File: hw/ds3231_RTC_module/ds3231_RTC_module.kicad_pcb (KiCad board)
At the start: 2 copper layers, 37 x 25 mm, 23 parts, among them J101 Conn_01x07, Q2101 AO3401A, Q2102 DMG1013T, U2101 DS3231M, U2102 CAT24C256, U2103 DS3231MZ

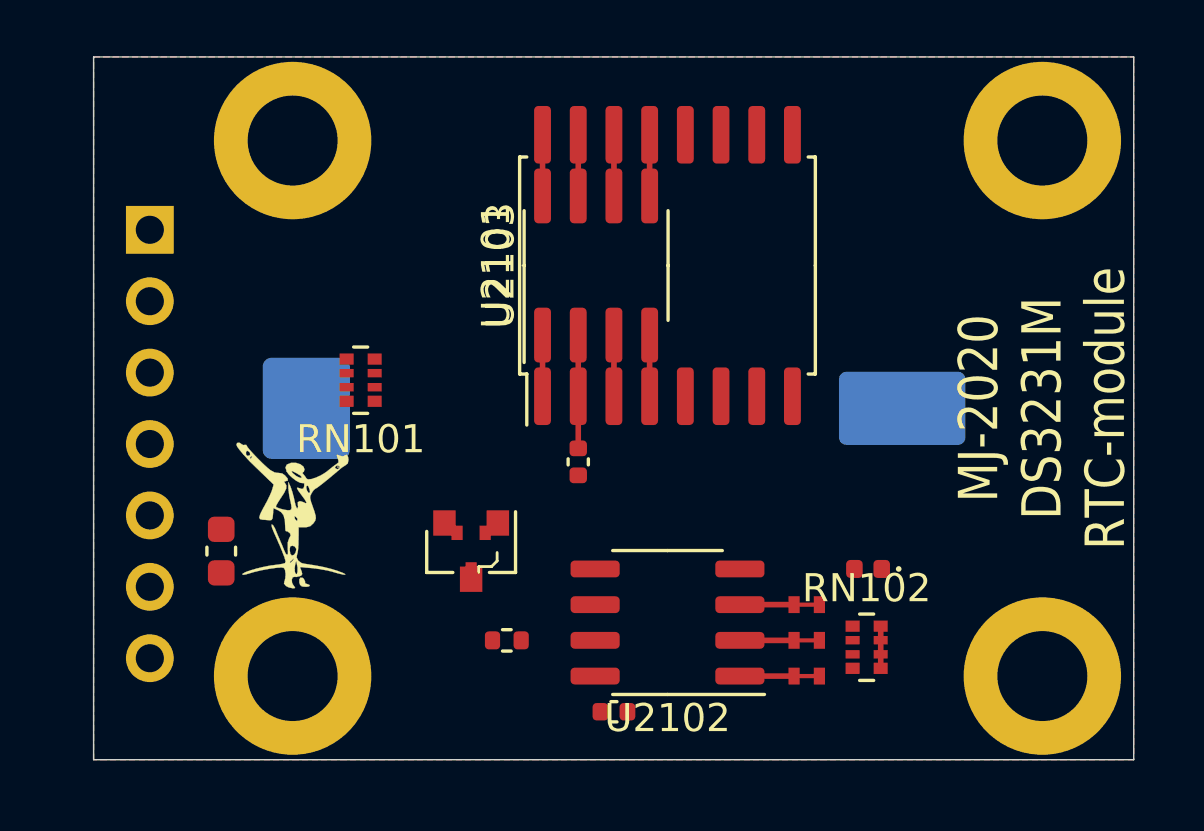
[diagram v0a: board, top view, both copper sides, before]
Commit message: Quick 1st layout & route of the RTC sub-module
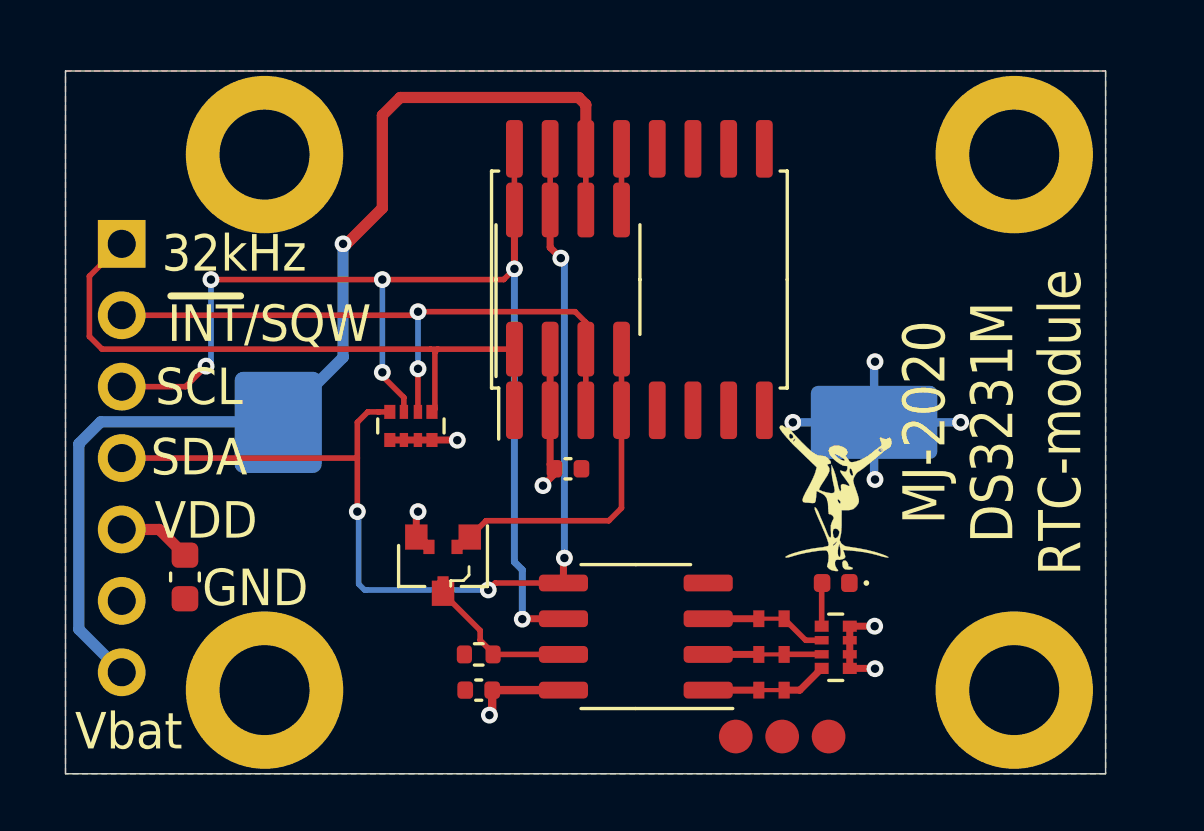
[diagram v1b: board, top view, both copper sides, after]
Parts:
- added REF**: KiCad-Logo_5mm_SilkScreen, Symbol:KiCad-Logo_5mm_SilkScreen, B.Cu at (70.0, 73.0)
- added TP101: TP, customlib_mj_fp:TP_SMD_1.2c, F.Cu at (73.8, 73.7)
- added TP102: TP, customlib_mj_fp:TP_SMD_1.2c, F.Cu at (77.1, 73.7)
- added TP103: TP, customlib_mj_fp:TP_SMD_1.2c, F.Cu at (75.5, 73.7)
- moved Logo101 19.3 mm to (77.4, 65.2)
- moved C2102 4.87 mm to (64.7, 72.0), turned to 0 degrees
- moved RN101 2.42 mm to (62.3, 62.6), turned to 270 degrees
- moved C101 1.58 mm to (54.2, 68.0)
- moved JP101 1.35 mm to (75.1, 72.0)
- moved JP102 1.35 mm to (75.1, 70.8)
- moved JP103 1.35 mm to (75.1, 69.5)
- moved D101 1.25 mm to (77.4, 68.2)
- moved U2102 1.23 mm to (70.3, 70.1)
- moved Q2101 1.12 mm to (63.4, 67.6)
- moved Q2102 1.12 mm to (63.4, 67.6)
- moved BT2101 1.12 mm to (70.4, 62.5)
- moved H101 1.12 mm to (57.1, 72.0)
- moved H102 1.12 mm to (83.8, 53.0)
- moved H103 1.12 mm to (57.1, 53.0)
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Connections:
- J101 pad 2: /~INT~-SQW -> /~INT~
- RN101 pad 2: /~INT~-SQW -> /~INT~
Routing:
- net /SCL: track 2.17 -> 40.7 mm, vias 0 -> 6
- net +BATT: track 2.17 -> 40.1 mm, vias 0 -> 1
- net /SDA: track 2.17 -> 38.6 mm, vias 0 -> 4
- net /32k: track 2.17 -> 23.6 mm
- net /~INT~: track 2.17 -> 23.4 mm, vias 0 -> 2
- net VDD: track 5.53 -> 18.4 mm, vias 0 -> 6
- net GND: track 2.17 -> 12.4 mm, vias 0 -> 4
- net /PG: track 2.17 -> 12.1 mm
- net /~WEn~: track 0.00 -> 5.77 mm
- net Net-(D101-Pad2): track 0.00 -> 1.54 mm
- net Net-(JP101-Pad1): track 2.83 -> 4.36 mm
- net Net-(JP103-Pad1): track 2.83 -> 4.35 mm
- net Net-(JP102-Pad1): track 2.83 -> 4.04 mm
- added copper zone on B.Cu, net VDD
- removed copper zone on B.Cu, net (none)
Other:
- board text added: "32kHz"
- board text added: "GND"
- board text added: "SCL"
- board text added: "SDA"
- board text added: "VDD"
- board text added: "Vbat"
- board text added: "~INT~/SQW"
